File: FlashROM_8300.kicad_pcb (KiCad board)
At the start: 2 copper layers, 16.4 x 39.3 mm, 8 parts, among them J1 uPD23C1000 / FLASH, U1 GLS29EE010 (TSOP), U2 SST39SF010 (TSOP), U3 SST39SF010 / GLS29EE010 (PLCC)

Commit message: minor tidying
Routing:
- removed copper zone on B.Cu, net /GND
- removed copper zone on F.Cu, net /GND

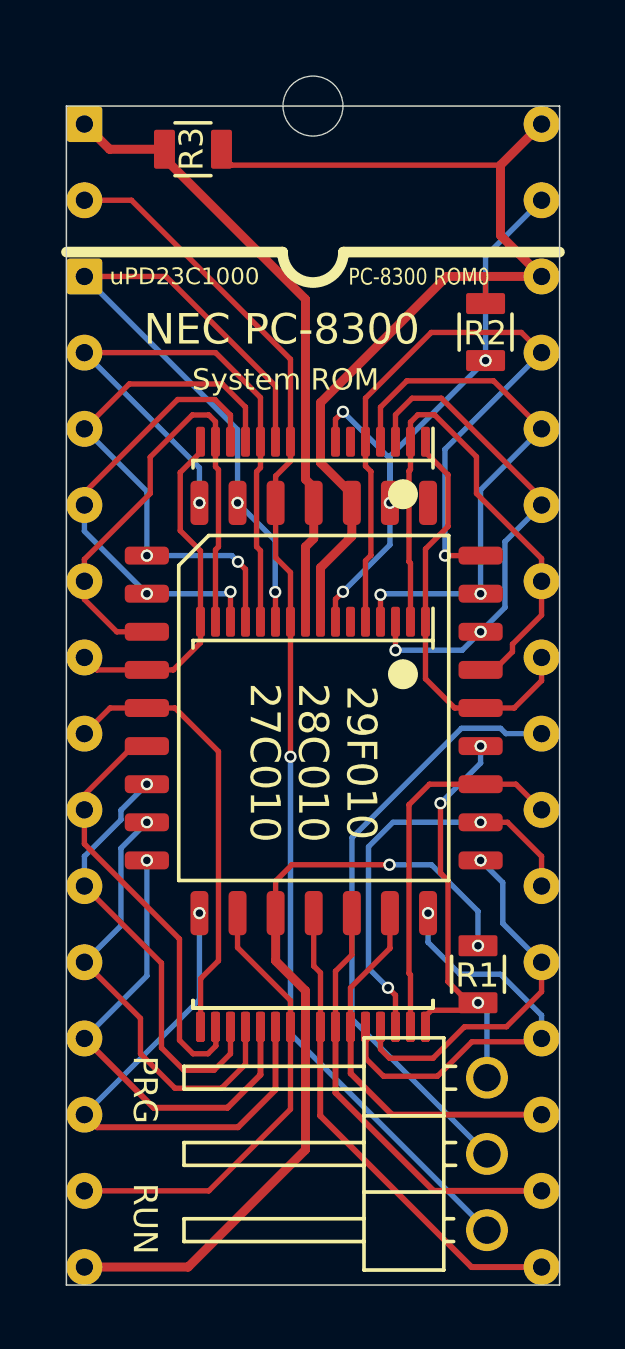
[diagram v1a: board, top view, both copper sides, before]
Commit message: uPD23C1000 & FlashROM_8300 correct A17 & A18 handling
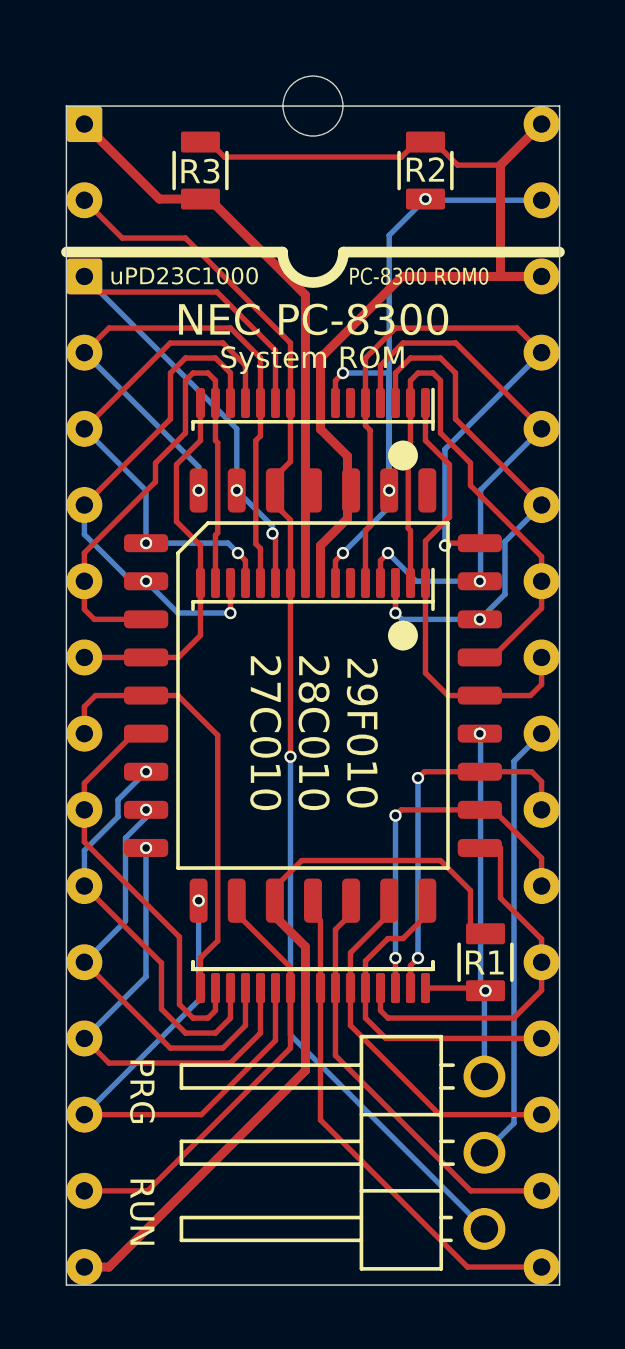
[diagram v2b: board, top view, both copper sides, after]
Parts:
- U1: value GLS29EE010 (TSOP) -> 29F010 TSOP-32 20mm
- U2: value SST39SF010 (TSOP) -> 29F010 sTSOP-32 14mm
- U3: value SST39SF010 / GLS29EE010 (PLCC) -> 29F010 PLCC 7x9
- moved R2 5.74 mm to (153.8, 80.0)
- moved U1 1.29 mm to (150.0, 97.5)
- moved U2 1.29 mm to (150.0, 100.5)
- moved R3 0.75 mm to (146.2, 80.0), turned to 90 degrees
- moved R1 0.47 mm to (155.8, 106.3)
- moved U3 0.42 mm to (150.0, 97.5)
- moved JP1 0.09 mm to (155.7, 115.2)
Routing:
- net /A16_~OE: track 20.3 -> 14.8 mm
- net /D6: track 14.4 -> 11.4 mm, vias 1 -> 0
- net /~WE: track 21.7 -> 24.5 mm
- net /A15: track 23.9 -> 22.0 mm
- net /~CE: track 13.9 -> 12.3 mm
- net /A6: track 15.3 -> 16.9 mm
- net /A5: track 17.8 -> 19.2 mm
- net /GND: track 27.1 -> 25.7 mm, vias 2 -> 0
- net /VPP: track 20.9 -> 19.6 mm
- net /~OE: track 14.7 -> 13.6 mm, vias 3 -> 2
- net /A9: track 18.7 -> 19.7 mm
- net /A11: track 13.9 -> 14.9 mm
- net /A4: track 11.7 -> 12.6 mm
- net /A0: track 14.9 -> 14.0 mm
- net /A8: track 16.7 -> 17.6 mm
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
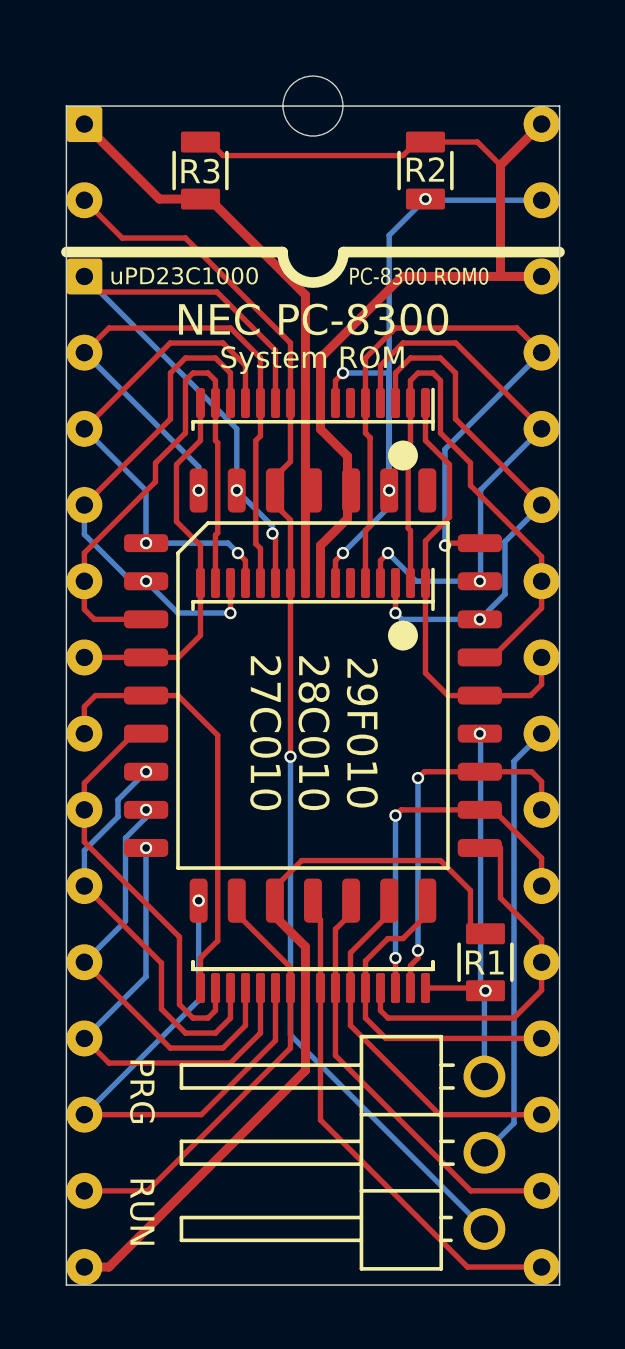
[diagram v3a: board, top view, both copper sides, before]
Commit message: FlexROM_100 & FlashROM_100 fix ALE/WE
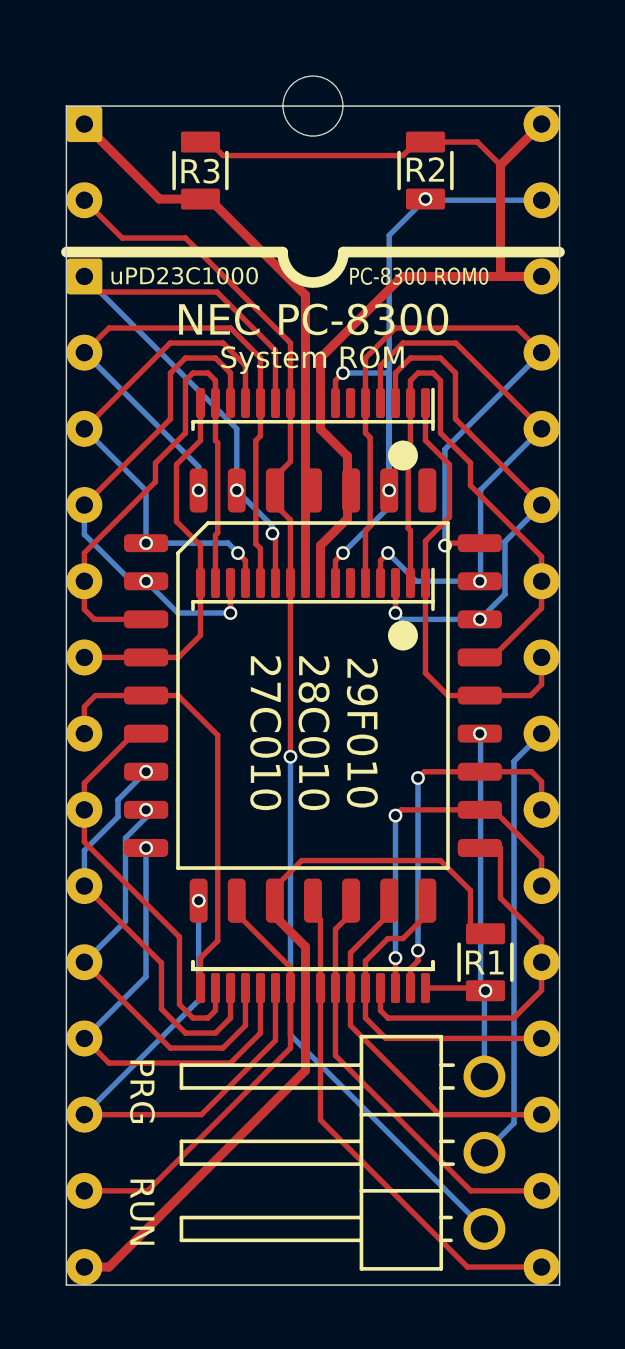
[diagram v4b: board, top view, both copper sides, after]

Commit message: simpler programming adapters, update pics and BOMs
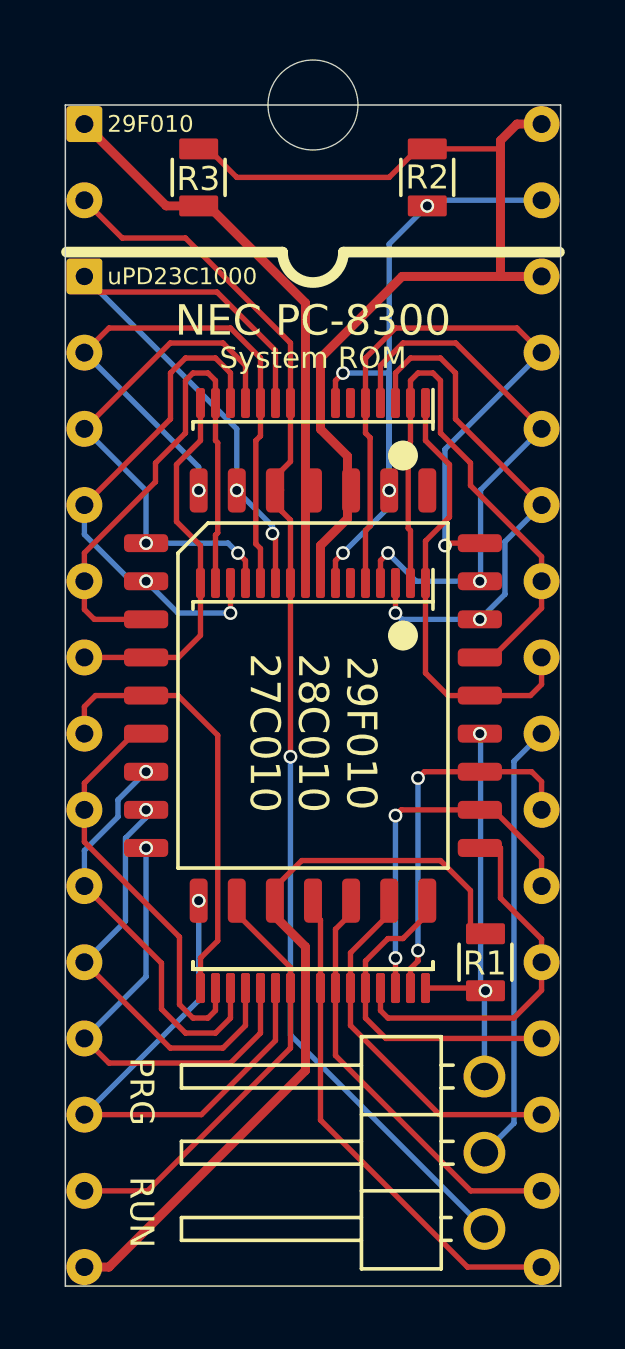
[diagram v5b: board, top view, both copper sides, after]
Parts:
- added REF**: NPTH_3mm, 000_LOCAL:NPTH_3mm, F.Cu at (150.0, 77.8)
- moved R2 0.24 mm to (153.8, 80.2)
- moved R3 0.24 mm to (146.2, 80.2)
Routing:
- net /VCC: track 34.5 -> 35.3 mm
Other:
- board size 16.4 x 39.3 mm -> 16.5 x 39.4 mm
- board text added: "29F010"
- board text removed: "PC-8300 ROM0"

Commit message: add FlashROM_100_tsop
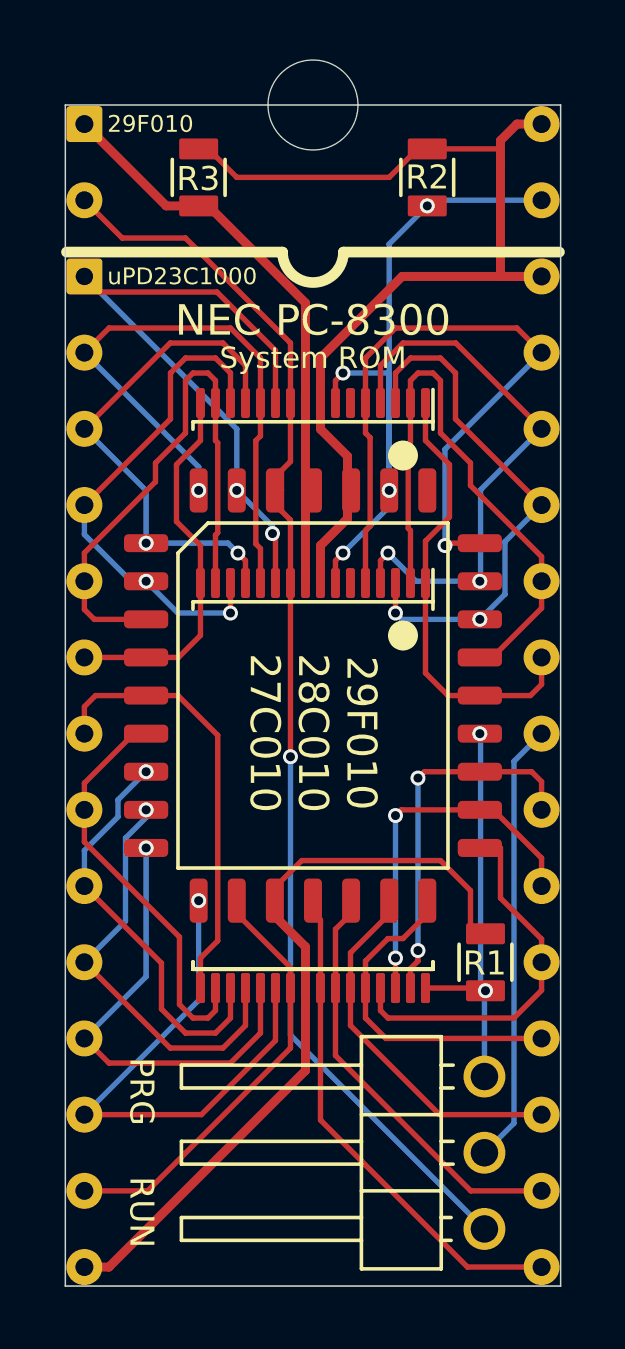
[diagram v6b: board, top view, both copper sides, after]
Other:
- net class Default: via_dia 0.41 -> 0.5; via_drill 0.25 -> 0.3
- rule via_min_drill: 0.25 -> 0.3
- rule via_min_size: 0.41 -> 0.5

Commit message: 0.3mm drills, gnd zone fills
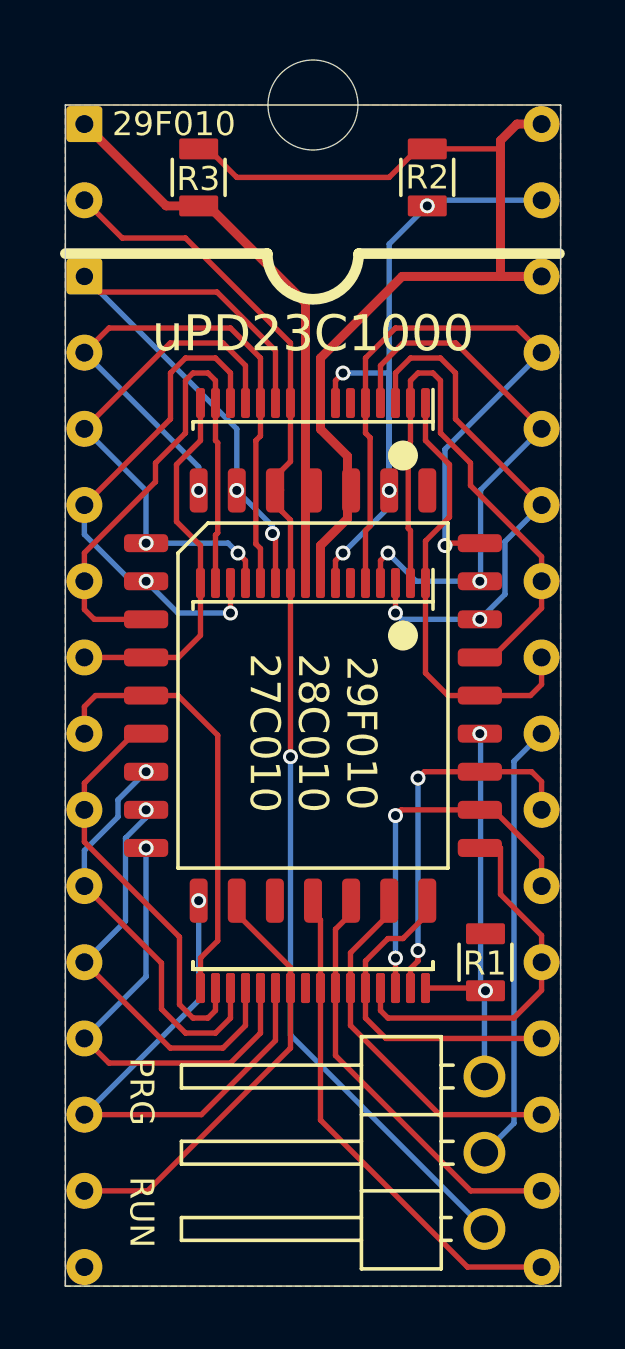
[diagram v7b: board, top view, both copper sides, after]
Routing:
- net /GND: track 25.7 -> 0.00 mm
- added copper zone on B.Cu, net /GND
- added copper zone on F.Cu, net /GND
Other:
- board text removed: "NEC PC-8300"
- board text removed: "System ROM"
